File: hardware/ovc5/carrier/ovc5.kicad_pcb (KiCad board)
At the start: 2 copper layers, 6 parts, among them J1 USB_C_Receptacle, U1 Mercury_XU5_4CG-4EV-5EV, U2 CYUSB43x7, U3 PICAM_Expandable, U4 PICAM_Expandable, U5 USB3_A_Dual_Stacked

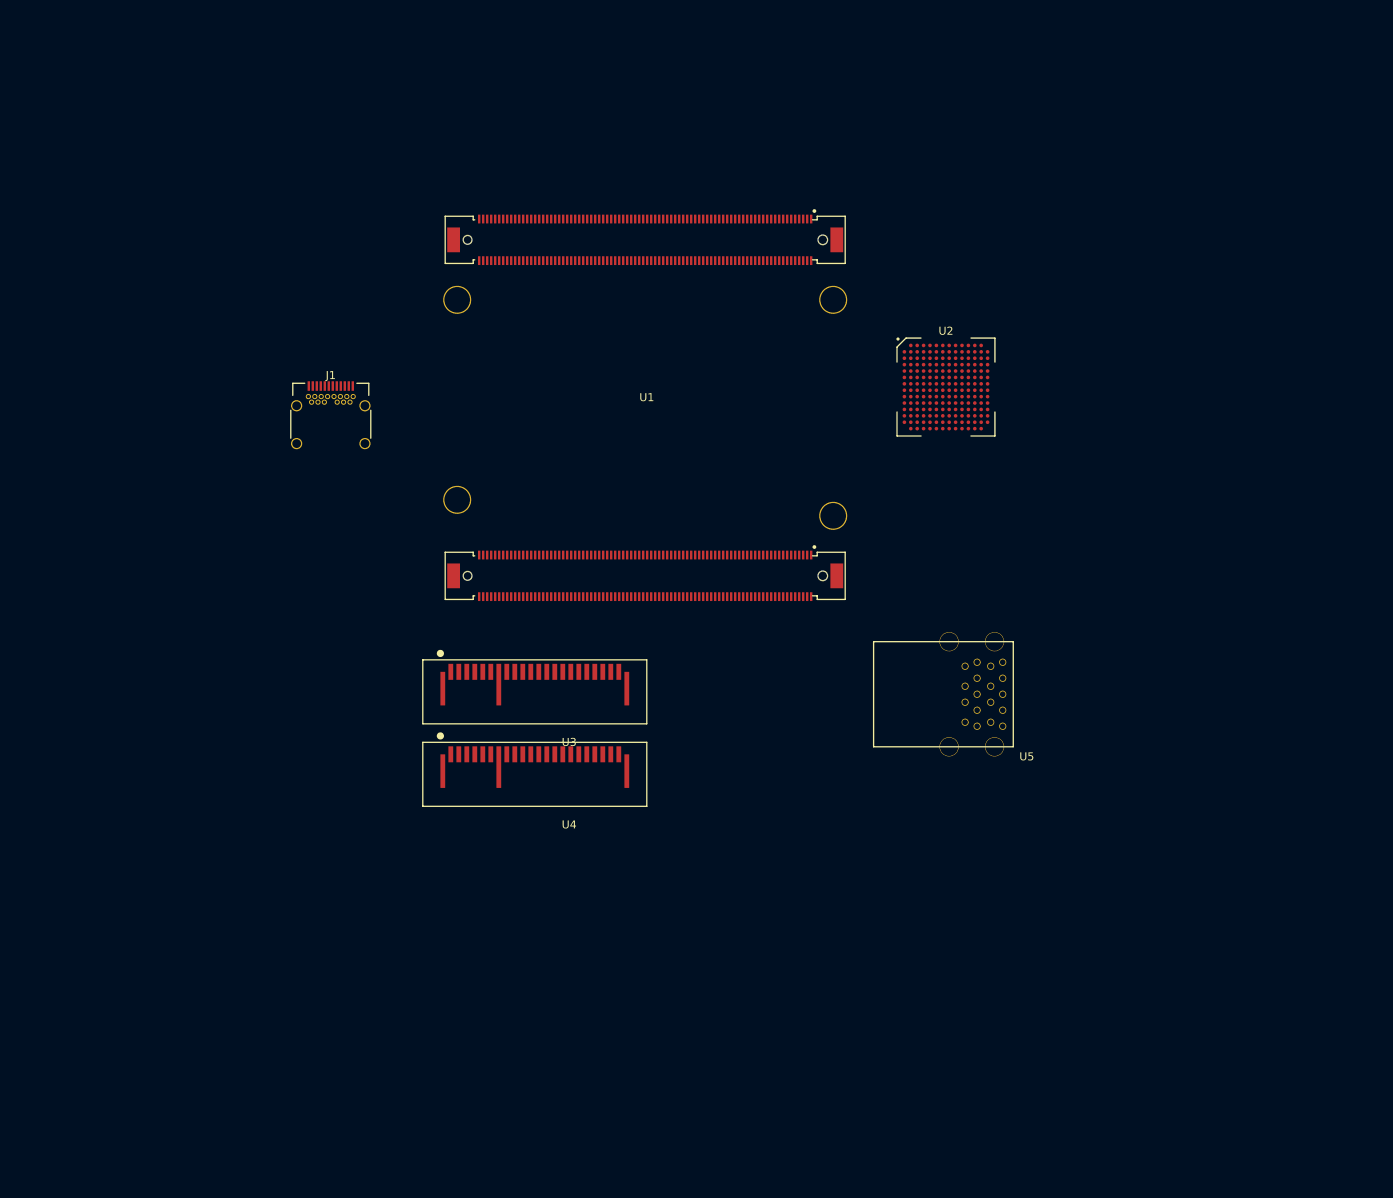
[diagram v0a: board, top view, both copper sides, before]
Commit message: Finish main schematics, start placing
Signed-off-by: Luca Della Vedova <luca@openrobotics.org>
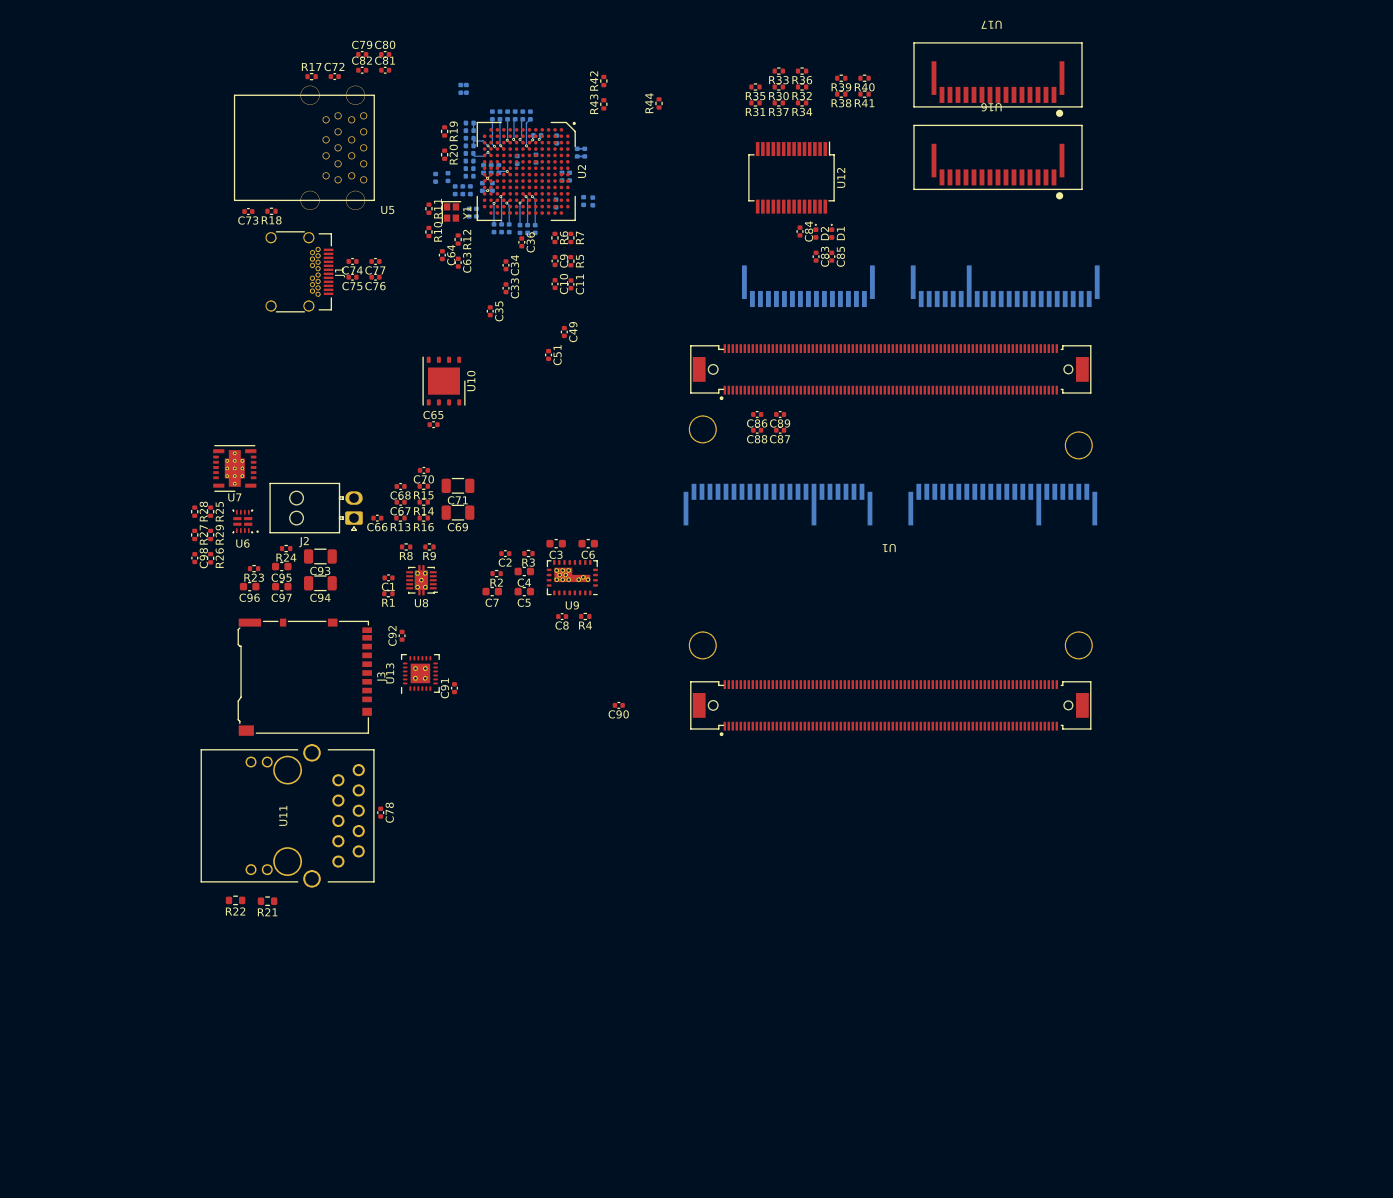
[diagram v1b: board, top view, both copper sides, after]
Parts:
- added C1: 100n, Capacitor_SMD:C_0402_1005Metric, F.Cu at (40.1, 77.8)
- added C10: 100n, Capacitor_SMD:C_0402_1005Metric, F.Cu at (60.9, 41.0)
- added C11: 100n, Capacitor_SMD:C_0402_1005Metric, F.Cu at (62.9, 41.1)
- added C12: 100n, Capacitor_SMD:C_0402_1005Metric, B.Cu at (54.0, 19.9)
- added C13: 100n, Capacitor_SMD:C_0402_1005Metric, B.Cu at (53.1, 19.9)
- added C14: 100n, Capacitor_SMD:C_0402_1005Metric, B.Cu at (56.0, 19.9)
- added C15: 100n, Capacitor_SMD:C_0402_1005Metric, B.Cu at (56.9, 19.9)
- added C16: 100n, Capacitor_SMD:C_0402_1005Metric, B.Cu at (56.5, 34.1)
- added C17: 100n, Capacitor_SMD:C_0402_1005Metric, B.Cu at (57.5, 34.1)
- added C18: 100n, Capacitor_SMD:C_0402_1005Metric, B.Cu at (53.3, 34.0)
- added C19: 100n, Capacitor_SMD:C_0402_1005Metric, B.Cu at (54.2, 34.0)
- added C2: 1u, Capacitor_SMD:C_0402_1005Metric, F.Cu at (54.7, 74.7)
- added C20: 100n, Capacitor_SMD:C_0402_1005Metric, B.Cu at (55.2, 34.0)
- added C21: 100n, Capacitor_SMD:C_0402_1005Metric, B.Cu at (55.0, 19.9)
- added C22: 100n, Capacitor_SMD:C_0402_1005Metric, B.Cu at (58.5, 34.1)
- added C23: 100n, Capacitor_SMD:C_0402_1005Metric, B.Cu at (57.9, 19.9)
- added C24: 100n, Capacitor_SMD:C_0402_1005Metric, B.Cu at (53.9, 26.6)
- added C25: 10u, Capacitor_SMD:C_0402_1005Metric, B.Cu at (53.1, 28.9)
- added C26: 10n, Capacitor_SMD:C_0402_1005Metric, B.Cu at (51.9, 28.9)
- added C27: 10n, Capacitor_SMD:C_0402_1005Metric, B.Cu at (53.0, 26.6)
- added C28: 10n, Capacitor_SMD:C_0402_1005Metric, B.Cu at (52.0, 26.6)
- added C29: 4u7, Capacitor_SMD:C_0402_1005Metric, B.Cu at (50.3, 22.8)
- added C3: 22u, Capacitor_SMD:C_0603_1608Metric, F.Cu at (61.1, 73.5)
- added C30: 100n, Capacitor_SMD:C_0402_1005Metric, B.Cu at (50.3, 23.8)
- added C31: 4u7, Capacitor_SMD:C_0402_1005Metric, B.Cu at (50.3, 20.9)
- added C32: 100n, Capacitor_SMD:C_0402_1005Metric, B.Cu at (50.3, 21.9)
- added C33: 1u, Capacitor_SMD:C_0402_1005Metric, F.Cu at (54.8, 41.5)
- added C34: 10u, Capacitor_SMD:C_0402_1005Metric, F.Cu at (54.8, 38.7)
- added C35: 1u, Capacitor_SMD:C_0402_1005Metric, F.Cu at (52.8, 44.4)
- added C36: 100n, Capacitor_SMD:C_0402_1005Metric, F.Cu at (56.8, 35.8)
- added C37: 100n, Capacitor_SMD:C_0402_1005Metric, B.Cu at (50.2, 24.7)
- added C38: 100n, Capacitor_SMD:C_0402_1005Metric, B.Cu at (50.2, 25.6)
- added C39: 100n, Capacitor_SMD:C_0402_1005Metric, B.Cu at (50.2, 26.6)
- added C4: 10p, Capacitor_SMD:C_0603_1608Metric, F.Cu at (57.1, 77.0)
- added C40: 100n, Capacitor_SMD:C_0402_1005Metric, B.Cu at (50.2, 27.6)
- added C41: 100n, Capacitor_SMD:C_0402_1005Metric, B.Cu at (61.1, 22.9)
- added C42: 100n, Capacitor_SMD:C_0402_1005Metric, B.Cu at (61.0, 30.9)
- added C43: 100n, Capacitor_SMD:C_0402_1005Metric, B.Cu at (46.0, 27.8)
- added C44: 100n, Capacitor_SMD:C_0402_1005Metric, B.Cu at (50.2, 32.1)
- added C45: 100n, Capacitor_SMD:C_0402_1005Metric, B.Cu at (49.4, 29.3)
- added C46: 10n, Capacitor_SMD:C_0402_1005Metric, B.Cu at (50.4, 29.3)
- added C47: 10u, Capacitor_SMD:C_0402_1005Metric, B.Cu at (48.5, 29.3)
- added C48: 100n, Capacitor_SMD:C_0402_1005Metric, B.Cu at (49.1, 16.6)
- added C49: 100n, Capacitor_SMD:C_0402_1005Metric, F.Cu at (62.1, 47.0)
- added C5: 22u, Capacitor_SMD:C_0603_1608Metric, F.Cu at (57.1, 79.5)
- added C50: 100n, Capacitor_SMD:C_0402_1005Metric, B.Cu at (58.7, 22.4)
- added C51: 10n, Capacitor_SMD:C_0402_1005Metric, F.Cu at (60.1, 49.9)
- added C52: 100n, Capacitor_SMD:C_0402_1005Metric, B.Cu at (64.5, 30.6)
- added C53: 100n, Capacitor_SMD:C_0402_1005Metric, B.Cu at (51.1, 32.1)
- added C54: 100n, Capacitor_SMD:C_0402_1005Metric, B.Cu at (49.9, 16.6)
- added C55: 1u, Capacitor_SMD:C_0402_1005Metric, B.Cu at (62.8, 27.6)
- added C56: 100n, Capacitor_SMD:C_0402_1005Metric, B.Cu at (61.8, 27.6)
- added C57: 100n, Capacitor_SMD:C_0402_1005Metric, B.Cu at (56.2, 25.5)
- added C58: 1u, Capacitor_SMD:C_0402_1005Metric, B.Cu at (64.7, 24.6)
- added C59: 100n, Capacitor_SMD:C_0402_1005Metric, B.Cu at (58.5, 25.4)
- added C6: 22u, Capacitor_SMD:C_0603_1608Metric, F.Cu at (65.1, 73.5)
- added C60: 100n, Capacitor_SMD:C_0402_1005Metric, B.Cu at (63.7, 24.6)
- added C61: 100n, Capacitor_SMD:C_0402_1005Metric, B.Cu at (65.7, 30.7)
- added C62: 4u7, Capacitor_SMD:C_0402_1005Metric, B.Cu at (47.5, 27.6)
- added C63: 12pF, Capacitor_SMD:C_0402_1005Metric, F.Cu at (48.8, 38.4)
- added C64: 12pF, Capacitor_SMD:C_0402_1005Metric, F.Cu at (46.8, 37.4)
- added C65: 100n, Capacitor_SMD:C_0402_1005Metric, F.Cu at (45.8, 58.6)
- added C66: 100n, Capacitor_SMD:C_0402_1005Metric, F.Cu at (38.7, 70.3)
- added C67: 100n, Capacitor_SMD:C_0402_1005Metric, F.Cu at (41.6, 68.3)
- added C68: 100n, Capacitor_SMD:C_0402_1005Metric, F.Cu at (41.6, 66.3)
- added C69: 100u, Capacitor_SMD:C_1206_3216Metric, F.Cu at (48.8, 69.6)
- added C7: 22u, Capacitor_SMD:C_0603_1608Metric, F.Cu at (53.1, 79.5)
- added C70: 100n, Capacitor_SMD:C_0402_1005Metric, F.Cu at (44.5, 64.3)
- added C71: 100u, Capacitor_SMD:C_1206_3216Metric, F.Cu at (48.8, 66.2)
- added C72: 2n2, Capacitor_SMD:C_0402_1005Metric, F.Cu at (33.4, 15.1)
- added C73: 2n2, Capacitor_SMD:C_0402_1005Metric, F.Cu at (22.6, 32.0)
- added C74: 100n, Capacitor_SMD:C_0402_1005Metric, F.Cu at (35.6, 38.2)
- added C75: 100n, Capacitor_SMD:C_0402_1005Metric, F.Cu at (35.6, 40.2)
- added C76: 100n, Capacitor_SMD:C_0402_1005Metric, F.Cu at (38.5, 40.2)
- added C77: 100n, Capacitor_SMD:C_0402_1005Metric, F.Cu at (38.5, 38.2)
- added C78: 100n, Capacitor_SMD:C_0402_1005Metric, F.Cu at (39.1, 107.1)
- added C79: 100n, Capacitor_SMD:C_0402_1005Metric, F.Cu at (36.8, 12.3)
- added C8: 100n, Capacitor_SMD:C_0402_1005Metric, F.Cu at (61.8, 82.6)
- added C80: 100n, Capacitor_SMD:C_0402_1005Metric, F.Cu at (39.7, 12.3)
- added C81: 100n, Capacitor_SMD:C_0402_1005Metric, F.Cu at (39.7, 14.3)
- added C82: 100n, Capacitor_SMD:C_0402_1005Metric, F.Cu at (36.8, 14.3)
- added C83: 100n, Capacitor_SMD:C_0402_1005Metric, F.Cu at (93.6, 37.6)
- added C84: 100n, Capacitor_SMD:C_0402_1005Metric, F.Cu at (91.5, 34.5)
- added C85: 100n, Capacitor_SMD:C_0402_1005Metric, F.Cu at (95.5, 37.6)
- added C86: 100n, Capacitor_SMD:C_0402_1005Metric, F.Cu at (86.2, 57.3)
- added C87: 100n, Capacitor_SMD:C_0402_1005Metric, F.Cu at (89.1, 59.3)
- added C88: 100n, Capacitor_SMD:C_0402_1005Metric, F.Cu at (86.2, 59.3)
- added C89: 100n, Capacitor_SMD:C_0402_1005Metric, F.Cu at (89.1, 57.3)
- added C9: 1u, Capacitor_SMD:C_0402_1005Metric, F.Cu at (60.9, 38.1)
- added C90: 1u, Capacitor_SMD:C_0402_1005Metric, F.Cu at (68.9, 93.7)
- added C91: 100n, Capacitor_SMD:C_0402_1005Metric, F.Cu at (48.4, 91.5)
- added C92: 100n, Capacitor_SMD:C_0402_1005Metric, F.Cu at (41.8, 85.0)
- added C93: 10u, Capacitor_SMD:C_1206_3216Metric, F.Cu at (31.6, 75.1)
- added C94: 10u, Capacitor_SMD:C_1206_3216Metric, F.Cu at (31.6, 78.4)
- added C95: 22u, Capacitor_SMD:C_0603_1608Metric, F.Cu at (26.8, 76.3)
- added C96: 22u, Capacitor_SMD:C_0603_1608Metric, F.Cu at (22.8, 78.8)
- added C97: 22u, Capacitor_SMD:C_0603_1608Metric, F.Cu at (26.8, 78.8)
- added C98: 100n, Capacitor_SMD:C_0402_1005Metric, F.Cu at (15.9, 75.3)
- added D1: LED_Small, LED_SMD:LED_0402_1005Metric, F.Cu at (95.5, 34.7)
- added D2: LED_Small, LED_SMD:LED_0402_1005Metric, F.Cu at (93.5, 34.7)
- added J2: AUX_PWR, Connector_Molex:Molex_Nano-Fit_105313-xx02_1x02_P2.50mm_Horizontal, F.Cu at (35.8, 70.3)
- added J3: Micro_SD_Card_Det_Hirose_DM3AT, Connector_Card:microSD_HC_Hirose_DM3AT-SF-PEJM5, F.Cu at (29.7, 90.2)
- added R1: 47k, Resistor_SMD:R_0402_1005Metric, F.Cu at (40.1, 79.7)
- added R10: 20k, Resistor_SMD:R_0402_1005Metric, F.Cu at (45.2, 34.5)
- added R11: 100k, Resistor_SMD:R_0402_1005Metric, F.Cu at (45.2, 31.6)
- added R12: 100k, Resistor_SMD:R_0402_1005Metric, F.Cu at (48.8, 35.5)
- added R13: 10k, Resistor_SMD:R_0402_1005Metric, F.Cu at (41.6, 70.3)
- added R14: 1k, Resistor_SMD:R_0402_1005Metric, F.Cu at (44.5, 68.3)
- added R15: 10k, Resistor_SMD:R_0402_1005Metric, F.Cu at (44.5, 66.3)
- added R16: 1k, Resistor_SMD:R_0402_1005Metric, F.Cu at (44.5, 70.3)
- added R17: 100k, Resistor_SMD:R_0402_1005Metric, F.Cu at (30.5, 15.1)
- added R18: 100k, Resistor_SMD:R_0402_1005Metric, F.Cu at (25.5, 31.9)
- added R19: 5k1, Resistor_SMD:R_0402_1005Metric, F.Cu at (47.1, 21.9)
- added R2: 348k, Resistor_SMD:R_0402_1005Metric, F.Cu at (53.6, 77.2)
- added R20: 5k1, Resistor_SMD:R_0402_1005Metric, F.Cu at (47.1, 24.9)
- added R21: 110R, Resistor_SMD:R_0603_1608Metric, F.Cu at (25.0, 118.2)
- added R22: 110R, Resistor_SMD:R_0603_1608Metric, F.Cu at (21.0, 118.1)
- added R23: 10k, Resistor_SMD:R_0402_1005Metric, F.Cu at (23.3, 76.6)
- added R24: 2k43, Resistor_SMD:R_0402_1005Metric, F.Cu at (27.3, 74.1)
- added R25: 47k, Resistor_SMD:R_0402_1005Metric, F.Cu at (17.9, 69.5)
- added R26: 10k, Resistor_SMD:R_0402_1005Metric, F.Cu at (17.9, 75.3)
- added R27: 47k, Resistor_SMD:R_0402_1005Metric, F.Cu at (15.9, 72.4)
- added R28: 10k, Resistor_SMD:R_0402_1005Metric, F.Cu at (15.9, 69.5)
- added R29: 22k, Resistor_SMD:R_0402_1005Metric, F.Cu at (17.9, 72.4)
- added R3: 348k, Resistor_SMD:R_0402_1005Metric, F.Cu at (57.6, 74.7)
- added R30: 2k4, Resistor_SMD:R_0402_1005Metric, F.Cu at (88.9, 16.4)
- added R31: 2k4, Resistor_SMD:R_0402_1005Metric, F.Cu at (86.0, 18.4)
- added R32: 2k4, Resistor_SMD:R_0402_1005Metric, F.Cu at (91.8, 16.4)
- added R33: 2k4, Resistor_SMD:R_0402_1005Metric, F.Cu at (88.9, 14.4)
- added R34: 2k4, Resistor_SMD:R_0402_1005Metric, F.Cu at (91.8, 18.4)
- added R35: 2k4, Resistor_SMD:R_0402_1005Metric, F.Cu at (86.0, 16.4)
- added R36: 2k4, Resistor_SMD:R_0402_1005Metric, F.Cu at (91.8, 14.4)
- added R37: 2k4, Resistor_SMD:R_0402_1005Metric, F.Cu at (88.9, 18.4)
- added R38: 2k4, Resistor_SMD:R_0402_1005Metric, F.Cu at (96.7, 17.3)
- added R39: 2k4, Resistor_SMD:R_0402_1005Metric, F.Cu at (96.7, 15.3)
- added R4: 100k, Resistor_SMD:R_0402_1005Metric, F.Cu at (64.7, 82.6)
- added R40: 2k4, Resistor_SMD:R_0402_1005Metric, F.Cu at (99.6, 15.3)
- added R41: 2k4, Resistor_SMD:R_0402_1005Metric, F.Cu at (99.6, 17.3)
- added R42: 2k4, Resistor_SMD:R_0402_1005Metric, F.Cu at (67.0, 15.7)
- added R43: 2k4, Resistor_SMD:R_0402_1005Metric, F.Cu at (67.0, 18.6)
- added R44: 10k, Resistor_SMD:R_0402_1005Metric, F.Cu at (73.9, 18.4)
- added R5: 20k, Resistor_SMD:R_0402_1005Metric, F.Cu at (62.9, 38.2)
- added R6: 10k, Resistor_SMD:R_0402_1005Metric, F.Cu at (60.9, 35.3)
- added R7: 10k, Resistor_SMD:R_0402_1005Metric, F.Cu at (62.9, 35.3)
- added R8: 100k, Resistor_SMD:R_0402_1005Metric, F.Cu at (42.3, 73.9)
- added R9: 100k, Resistor_SMD:R_0402_1005Metric, F.Cu at (45.2, 73.9)
- added U10: S25FL064, Package_SON:WSON-8-1EP_6x5mm_P1.27mm_EP3.4x4mm, F.Cu at (47.0, 53.2)
- added U11: ARJ11C-MBSAS-A-BA-7MU2, Ethernet:ARJ11C-MBSAS-A-BA-7MU2, F.Cu at (27.5, 107.5)
- added U12: FT232RL, Package_SO:SSOP-28_5.3x10.2mm_P0.65mm, F.Cu at (90.5, 27.8)
- added U13: TXS02612, WQFN:TI_RTW0024B, F.Cu at (44.1, 89.7)
- added U14: PICAM, Connectors_OSRF:AMPHENOL_SFW15R, B.Cu at (92.4, 39.8)
- added U15: PICAM_Expandable, Connectors_OSRF:AMPHENOL_SFW15R+SFW21R, B.Cu at (88.9, 70.0)
- added U16: PICAM, Connectors_OSRF:AMPHENOL_SFW15R, F.Cu at (116.5, 24.6)
- added U17: PICAM, Connectors_OSRF:AMPHENOL_SFW15R, F.Cu at (116.5, 14.3)
- added U6: TPS2121, TI:Texas_VQFN-HR-12_2x2.5_Pitch0.5mm, F.Cu at (21.9, 70.7)
- added U7: TPSM53604RDA, Package_DFN_QFN:Texas_B3QFN-14-1EP_5x5.5mm_P0.65mm_ThermalVia, F.Cu at (20.9, 64.1)
- added U8: TPS2561, Package_SON:VSON-10-1EP_3x3mm_P0.5mm_EP1.65x2.4mm_ThermalVias, F.Cu at (44.2, 78.0)
- added U9: EN5339QI, DCDC:Converter_DCDC_Intel_QFN-24_4x6mm_P0.65mm_ThermalVias, F.Cu at (63.1, 77.7)
- added Y1: 25MHz, Crystal:Crystal_SMD_2016-4Pin_2.0x1.6mm, F.Cu at (48.0, 32.1)
- U3, U4: moved to B.Cu
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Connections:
- net Net-(J1-PadA4) renamed VBUS
- J1 pad A1: Net-(J1-PadA1) -> GND
- J1 pad A10: unconnected-(J1-PadA10) -> /USB/USB_DS_RX2_N
- J1 pad A11: unconnected-(J1-PadA11) -> /USB/USB_DS_RX2_P
- J1 pad A12: Net-(J1-PadA1) -> GND
- J1 pad A2: unconnected-(J1-PadA2) -> Net-(J1-PadA2)
- J1 pad A3: unconnected-(J1-PadA3) -> Net-(J1-PadA3)
- J1 pad A5: unconnected-(J1-PadA5) -> /USB/USB_DS_CC1
- J1 pad A6: unconnected-(J1-PadA6) -> /USB/USB_DS_D_P
- J1 pad A7: unconnected-(J1-PadA7) -> /USB/USB_DS_D_N
- J1 pad B1: Net-(J1-PadA1) -> GND
- J1 pad B10: unconnected-(J1-PadB10) -> /USB/USB_DS_RX1_N
- J1 pad B11: unconnected-(J1-PadB11) -> /USB/USB_DS_RX1_P
- J1 pad B12: Net-(J1-PadA1) -> GND
- J1 pad B2: unconnected-(J1-PadB2) -> Net-(J1-PadB2)
- J1 pad B3: unconnected-(J1-PadB3) -> Net-(J1-PadB3)
- J1 pad B5: unconnected-(J1-PadB5) -> /USB/USB_DS_CC2
- J1 pad B6: unconnected-(J1-PadB6) -> /USB/USB_DS_D_P
- J1 pad B7: unconnected-(J1-PadB7) -> /USB/USB_DS_D_N
- J1 pad S1: unconnected-(J1-PadS1) -> Net-(C73-Pad1)
- U1 pad A101: unconnected-(U1-PadA101) -> SDIO_D2
- U1 pad A103: unconnected-(U1-PadA103) -> SDIO_D3
- U1 pad A105: unconnected-(U1-PadA105) -> DEBUG_UART_RX
- U1 pad A107: unconnected-(U1-PadA107) -> DEBUG_UART_TX
- U1 pad A108: unconnected-(U1-PadA108) -> GND
- U1 pad A109: unconnected-(U1-PadA109) -> GND
- U1 pad A120: unconnected-(U1-PadA120) -> GND
- U1 pad A125: unconnected-(U1-PadA125) -> GND
- U1 pad A127: unconnected-(U1-PadA127) -> FPGA_USB0_D+
- U1 pad A129: unconnected-(U1-PadA129) -> FPGA_USB0_D-
- U1 pad A13: unconnected-(U1-PadA13) -> GND
- U1 pad A131: unconnected-(U1-PadA131) -> FPGA_USB1_D+
- U1 pad A133: unconnected-(U1-PadA133) -> FPGA_USB1_D-
- U1 pad A134: unconnected-(U1-PadA134) -> GND
- U1 pad A135: unconnected-(U1-PadA135) -> GND
- U1 pad A138: unconnected-(U1-PadA138) -> GND
- U1 pad A139: unconnected-(U1-PadA139) -> GND
- U1 pad A14: unconnected-(U1-PadA14) -> GND
- U1 pad A142: unconnected-(U1-PadA142) -> GND
- U1 pad A143: unconnected-(U1-PadA143) -> GND
- U1 pad A145: unconnected-(U1-PadA145) -> GBE_MDI3_N
- U1 pad A147: unconnected-(U1-PadA147) -> CAM3_DAT3-
- U1 pad A149: unconnected-(U1-PadA149) -> GBE_LED_ACT
- U1 pad A151: unconnected-(U1-PadA151) -> GBE_MDI2_N
- U1 pad A153: unconnected-(U1-PadA153) -> GBE_MDI2_P
- U1 pad A157: unconnected-(U1-PadA157) -> GBE_MDI1_N
- U1 pad A159: unconnected-(U1-PadA159) -> GBE_MDI1_P
- U1 pad A161: unconnected-(U1-PadA161) -> GBE_LED_LINK
- U1 pad A163: unconnected-(U1-PadA163) -> GBE_MDI0_N
- U1 pad A165: unconnected-(U1-PadA165) -> GBE_MDI0_P
- U1 pad A166: unconnected-(U1-PadA166) -> GND
- U1 pad A167: unconnected-(U1-PadA167) -> GND
- U1 pad A20: unconnected-(U1-PadA20) -> GND
- U1 pad A23: unconnected-(U1-PadA23) -> GND
- U1 pad A26: unconnected-(U1-PadA26) -> +3V3
- U1 pad A29: unconnected-(U1-PadA29) -> +3V3
- U1 pad A32: unconnected-(U1-PadA32) -> GND
- U1 pad A35: unconnected-(U1-PadA35) -> GND
- U1 pad A44: unconnected-(U1-PadA44) -> GND
- U1 pad A47: unconnected-(U1-PadA47) -> GND
- U1 pad A50: unconnected-(U1-PadA50) -> +3V3
- U1 pad A56: unconnected-(U1-PadA56) -> GND
- U1 pad A59: unconnected-(U1-PadA59) -> GND
- U1 pad A68: unconnected-(U1-PadA68) -> GND
- U1 pad A71: unconnected-(U1-PadA71) -> GND
- U1 pad A80: unconnected-(U1-PadA80) -> GND
- U1 pad A83: unconnected-(U1-PadA83) -> GND
- U1 pad A86: unconnected-(U1-PadA86) -> +3V3
- U1 pad A91: unconnected-(U1-PadA91) -> SDIO_CLK
- U1 pad A92: unconnected-(U1-PadA92) -> CAM3_SDA
- U1 pad A93: unconnected-(U1-PadA93) -> SDIO_CMD
- U1 pad A94: unconnected-(U1-PadA94) -> CAM3_SCL
- U1 pad A95: unconnected-(U1-PadA95) -> SDIO_D0
- U1 pad A96: unconnected-(U1-PadA96) -> GND
- U1 pad A97: unconnected-(U1-PadA97) -> SDIO_D1
- U1 pad A99: unconnected-(U1-PadA99) -> GND
- U1 pad B1: unconnected-(U1-PadB1) -> GND
- U1 pad B100: unconnected-(U1-PadB100) -> CAM4_CLK+
- U1 pad B101: unconnected-(U1-PadB101) -> CAM0_CLK+
- U1 pad B102: unconnected-(U1-PadB102) -> CAM4_CLK-
- U1 pad B103: unconnected-(U1-PadB103) -> CAM0_CLK-
- U1 pad B104: unconnected-(U1-PadB104) -> CAM1_TRIGGER
- U1 pad B105: unconnected-(U1-PadB105) -> GND
- U1 pad B106: unconnected-(U1-PadB106) -> CAM1_ENABLE
- U1 pad B107: unconnected-(U1-PadB107) -> CAM0_DAT0+
- U1 pad B108: unconnected-(U1-PadB108) -> +1V8
- U1 pad B109: unconnected-(U1-PadB109) -> CAM0_DAT0-
- U1 pad B11: unconnected-(U1-PadB11) -> GND
- U1 pad B110: unconnected-(U1-PadB110) -> CAM1_CLK+
- U1 pad B111: unconnected-(U1-PadB111) -> CAM0_DAT1+
- U1 pad B112: unconnected-(U1-PadB112) -> CAM1_CLK-
- U1 pad B113: unconnected-(U1-PadB113) -> CAM0_DAT1-
- U1 pad B114: unconnected-(U1-PadB114) -> CAM1_DAT0+
- U1 pad B115: unconnected-(U1-PadB115) -> +3V3
- U1 pad B116: unconnected-(U1-PadB116) -> CAM1_DAT0-
- U1 pad B117: unconnected-(U1-PadB117) -> CAM0_DAT3+
- U1 pad B118: unconnected-(U1-PadB118) -> GND
- U1 pad B119: unconnected-(U1-PadB119) -> CAM0_DAT3-
- U1 pad B120: unconnected-(U1-PadB120) -> CAM1_DAT1+
- U1 pad B121: unconnected-(U1-PadB121) -> GND
- U1 pad B122: unconnected-(U1-PadB122) -> CAM1_DAT1-
- U1 pad B123: unconnected-(U1-PadB123) -> CAM3_CLK+
- U1 pad B124: unconnected-(U1-PadB124) -> CAM1_SDA
- U1 pad B125: unconnected-(U1-PadB125) -> CAM3_CLK-
- U1 pad B126: unconnected-(U1-PadB126) -> CAM1_SCL
- U1 pad B127: unconnected-(U1-PadB127) -> +3V3
- U1 pad B128: unconnected-(U1-PadB128) -> +1V8
- U1 pad B129: unconnected-(U1-PadB129) -> CAM0_DAT2+
- U1 pad B130: unconnected-(U1-PadB130) -> CAM2_CLK+
- U1 pad B131: unconnected-(U1-PadB131) -> CAM0_DAT2-
- U1 pad B132: unconnected-(U1-PadB132) -> CAM2_CLK-
- U1 pad B133: unconnected-(U1-PadB133) -> CAM3_ENABLE
- U1 pad B134: unconnected-(U1-PadB134) -> GND
- U1 pad B135: unconnected-(U1-PadB135) -> CAM3_TRIGGER
- U1 pad B136: unconnected-(U1-PadB136) -> CAM1_DAT2+
- U1 pad B137: unconnected-(U1-PadB137) -> GND
- U1 pad B138: unconnected-(U1-PadB138) -> CAM1_DAT2-
- U1 pad B139: unconnected-(U1-PadB139) -> CAM2_SCL
- U1 pad B14: unconnected-(U1-PadB14) -> GND
- U1 pad B141: unconnected-(U1-PadB141) -> CAM2_SDA
- U1 pad B142: unconnected-(U1-PadB142) -> CAM1_DAT3+
- U1 pad B143: unconnected-(U1-PadB143) -> +1V8
- U1 pad B144: unconnected-(U1-PadB144) -> CAM1_DAT3-
- U1 pad B145: unconnected-(U1-PadB145) -> CAM3_DAT3+
- U1 pad B146: unconnected-(U1-PadB146) -> GND
- U1 pad B148: unconnected-(U1-PadB148) -> CAM4_DAT1+
- U1 pad B149: unconnected-(U1-PadB149) -> GND
- U1 pad B15: unconnected-(U1-PadB15) -> GND
- U1 pad B150: unconnected-(U1-PadB150) -> CAM4_DAT1-
- U1 pad B151: unconnected-(U1-PadB151) -> CAM3_DAT0+
- U1 pad B152: unconnected-(U1-PadB152) -> +3V3
- U1 pad B153: unconnected-(U1-PadB153) -> CAM3_DAT0-
- U1 pad B154: unconnected-(U1-PadB154) -> CAM2_DAT0+
- U1 pad B155: unconnected-(U1-PadB155) -> +3V3
- U1 pad B156: unconnected-(U1-PadB156) -> CAM2_DAT0-
- U1 pad B157: unconnected-(U1-PadB157) -> CAM3_DAT2+
- U1 pad B158: unconnected-(U1-PadB158) -> GND
- U1 pad B159: unconnected-(U1-PadB159) -> CAM3_DAT2-
- U1 pad B160: unconnected-(U1-PadB160) -> CAM2_DAT1+
- U1 pad B161: unconnected-(U1-PadB161) -> GND
- U1 pad B162: unconnected-(U1-PadB162) -> CAM2_DAT1-
- U1 pad B163: unconnected-(U1-PadB163) -> CAM3_DAT1+
- U1 pad B164: unconnected-(U1-PadB164) -> CAM4_DAT0+
- U1 pad B165: unconnected-(U1-PadB165) -> CAM3_DAT1-
- U1 pad B166: unconnected-(U1-PadB166) -> CAM4_DAT0-
- U1 pad B18: unconnected-(U1-PadB18) -> GND
- U1 pad B19: unconnected-(U1-PadB19) -> GND
- U1 pad B2: unconnected-(U1-PadB2) -> GND
- U1 pad B22: unconnected-(U1-PadB22) -> GND
- U1 pad B23: unconnected-(U1-PadB23) -> GND
- U1 pad B26: unconnected-(U1-PadB26) -> GND
- U1 pad B27: unconnected-(U1-PadB27) -> GND
- U1 pad B29: unconnected-(U1-PadB29) -> Net-(C86-Pad2)
- U1 pad B30: unconnected-(U1-PadB30) -> GND
- U1 pad B31: unconnected-(U1-PadB31) -> GND
- U1 pad B32: unconnected-(U1-PadB32) -> FPGA_USB0_RX+
- U1 pad B33: unconnected-(U1-PadB33) -> Net-(C87-Pad2)
- U1 pad B34: unconnected-(U1-PadB34) -> GND
- U1 pad B35: unconnected-(U1-PadB35) -> GND
- U1 pad B36: unconnected-(U1-PadB36) -> FPGA_USB0_RX-
- U1 pad B37: unconnected-(U1-PadB37) -> Net-(C88-Pad2)
- U1 pad B38: unconnected-(U1-PadB38) -> GND
- U1 pad B39: unconnected-(U1-PadB39) -> GND
- U1 pad B40: unconnected-(U1-PadB40) -> FPGA_USB1_RX+
- U1 pad B41: unconnected-(U1-PadB41) -> Net-(C89-Pad2)
- U1 pad B42: unconnected-(U1-PadB42) -> GND
- U1 pad B43: unconnected-(U1-PadB43) -> GND
- U1 pad B44: unconnected-(U1-PadB44) -> FPGA_USB1_RX-
- U1 pad B46: unconnected-(U1-PadB46) -> GND
- U1 pad B49: unconnected-(U1-PadB49) -> GND
- U1 pad B52: unconnected-(U1-PadB52) -> +1V8
- U1 pad B55: unconnected-(U1-PadB55) -> +3V3
- U1 pad B58: unconnected-(U1-PadB58) -> GND
- U1 pad B61: unconnected-(U1-PadB61) -> GND
- U1 pad B64: unconnected-(U1-PadB64) -> +1V8
- U1 pad B70: unconnected-(U1-PadB70) -> GND
- U1 pad B72: unconnected-(U1-PadB72) -> CAM2_TRIGGER
- U1 pad B73: unconnected-(U1-PadB73) -> GND
- U1 pad B74: unconnected-(U1-PadB74) -> CAM2_ENABLE
- U1 pad B75: unconnected-(U1-PadB75) -> CAM5_ENABLE
- U1 pad B76: unconnected-(U1-PadB76) -> +1V8
- U1 pad B77: unconnected-(U1-PadB77) -> CAM5_TRIGGER
- U1 pad B78: unconnected-(U1-PadB78) -> CAM5_SDA
- U1 pad B79: unconnected-(U1-PadB79) -> +3V3
- U1 pad B80: unconnected-(U1-PadB80) -> CAM5_SCL
- U1 pad B81: unconnected-(U1-PadB81) -> CAM4_ENABLE
- U1 pad B82: unconnected-(U1-PadB82) -> GND
- U1 pad B83: unconnected-(U1-PadB83) -> CAM4_TRIGGER
- U1 pad B84: unconnected-(U1-PadB84) -> CAM5_CLK+
- U1 pad B85: unconnected-(U1-PadB85) -> GND
- U1 pad B86: unconnected-(U1-PadB86) -> CAM5_CLK-
- U1 pad B87: unconnected-(U1-PadB87) -> CAM4_SCL
- U1 pad B88: unconnected-(U1-PadB88) -> +1V8
- U1 pad B89: unconnected-(U1-PadB89) -> CAM4_SDA
- U1 pad B90: unconnected-(U1-PadB90) -> CAM5_DAT0+
- U1 pad B91: unconnected-(U1-PadB91) -> CAM0_SCL
- U1 pad B92: unconnected-(U1-PadB92) -> CAM5_DAT0-
- U1 pad B93: unconnected-(U1-PadB93) -> CAM0_SDA
- U1 pad B94: unconnected-(U1-PadB94) -> CAM5_DAT1+
- U1 pad B95: unconnected-(U1-PadB95) -> +1V8
- U1 pad B96: unconnected-(U1-PadB96) -> CAM5_DAT1-
- U1 pad B97: unconnected-(U1-PadB97) -> CAM0_ENABLE
- U1 pad B98: unconnected-(U1-PadB98) -> GND
- U1 pad B99: unconnected-(U1-PadB99) -> CAM0_TRIGGER
- U2 pad A10: unconnected-(U2-PadA10) -> /USB/USB_SPI_DO
- U2 pad A11: unconnected-(U2-PadA11) -> /USB/USB_SP_nWP
- U2 pad A12: unconnected-(U2-PadA12) -> USB_UART_D-
- U2 pad A13: unconnected-(U2-PadA13) -> USB_UART_D+
- U2 pad A5: unconnected-(U2-PadA5) -> +3V3
- U2 pad A6: unconnected-(U2-PadA6) -> Net-(U2-PadA6)
- U2 pad A7: unconnected-(U2-PadA7) -> Net-(U2-PadA7)
- U2 pad B1: unconnected-(U2-PadB1) -> FPGA_USB0_D-
- U2 pad B10: unconnected-(U2-PadB10) -> /USB/USB_SPI_CS
- U2 pad B13: unconnected-(U2-PadB13) -> FPGA_USB1_D-
- U2 pad B14: unconnected-(U2-PadB14) -> FPGA_USB1_D+
- U2 pad B2: unconnected-(U2-PadB2) -> FPGA_USB0_D+
- U2 pad B3: unconnected-(U2-PadB3) -> /USB/USB_DS_CC2
- U2 pad B5: unconnected-(U2-PadB5) -> /USB/VBUS_MON_P1
- U2 pad B6: unconnected-(U2-PadB6) -> Net-(U2-PadB6)
- U2 pad C1: unconnected-(U2-PadC1) -> FPGA_USB0_TX+
- U2 pad C11: unconnected-(U2-PadC11) -> /USB/XRES_DMC
- U2 pad C12: unconnected-(U2-PadC12) -> +3V3
- U2 pad C2: unconnected-(U2-PadC2) -> FPGA_USB0_TX-
- U2 pad C3: unconnected-(U2-PadC3) -> +3V3
- U2 pad C4: unconnected-(U2-PadC4) -> +5V
- U2 pad C6: unconnected-(U2-PadC6) -> +3V3
- U2 pad C9: unconnected-(U2-PadC9) -> +3V3
- U2 pad D1: unconnected-(U2-PadD1) -> FPGA_USB0_RX+
- U2 pad D11: unconnected-(U2-PadD11) -> /USB/USB_I2C_SDA
- U2 pad D12: unconnected-(U2-PadD12) -> /USB/USB_SPI_CLK
- U2 pad D2: unconnected-(U2-PadD2) -> FPGA_USB0_RX-
- U2 pad D3: unconnected-(U2-PadD3) -> /USB/USB_DS_CC1
- U2 pad D4: unconnected-(U2-PadD4) -> /USB/VBUS_MON_P0
- U2 pad D5: unconnected-(U2-PadD5) -> Net-(U2-PadD5)
- U2 pad D7: unconnected-(U2-PadD7) -> +5V
- U2 pad D8: unconnected-(U2-PadD8) -> /USB/USB_US0_CC1
- U2 pad D9: unconnected-(U2-PadD9) -> Net-(U2-PadD9)
- U2 pad E10: unconnected-(U2-PadE10) -> GND
- U2 pad E11: unconnected-(U2-PadE11) -> /USB/USB_I2C_SCL
- U2 pad E13: unconnected-(U2-PadE13) -> FPGA_USB1_RX-
- U2 pad E14: unconnected-(U2-PadE14) -> FPGA_USB1_RX+
- U2 pad E7: unconnected-(U2-PadE7) -> +5V
- U2 pad E8: unconnected-(U2-PadE8) -> +3V3
- U2 pad F10: unconnected-(U2-PadF10) -> +3V3
- U2 pad F11: unconnected-(U2-PadF11) -> /USB/VDD10
- U2 pad F12: unconnected-(U2-PadF12) -> /USB/USB_SPI_DI
- U2 pad F13: unconnected-(U2-PadF13) -> FPGA_USB1_TX-
- U2 pad F14: unconnected-(U2-PadF14) -> FPGA_USB1_TX+
- U2 pad F4: unconnected-(U2-PadF4) -> /USB/VDD10
- U2 pad F5: unconnected-(U2-PadF5) -> Net-(U2-PadD5)
- U2 pad F6: unconnected-(U2-PadF6) -> GND
- U2 pad F7: unconnected-(U2-PadF7) -> GND
- U2 pad F8: unconnected-(U2-PadF8) -> GND
- U2 pad F9: unconnected-(U2-PadF9) -> GND
- U2 pad G1: unconnected-(U2-PadG1) -> /USB/USB_H1_TX_P
- U2 pad G10: unconnected-(U2-PadG10) -> /USB/USB_I2C_SDA
- U2 pad G11: unconnected-(U2-PadG11) -> /USB/1V0_PHY
- U2 pad G12: unconnected-(U2-PadG12) -> +3V3
- U2 pad G13: unconnected-(U2-PadG13) -> /USB/USB_H0_RX_N
- U2 pad G14: unconnected-(U2-PadG14) -> /USB/USB_H0_RX_P
- U2 pad G2: unconnected-(U2-PadG2) -> /USB/USB_H1_TX_N
- U2 pad G3: unconnected-(U2-PadG3) -> +3V3
- U2 pad G4: unconnected-(U2-PadG4) -> /USB/1V0_PHY
- U2 pad G5: unconnected-(U2-PadG5) -> +3V3
- U2 pad G6: unconnected-(U2-PadG6) -> GND
- U2 pad G7: unconnected-(U2-PadG7) -> GND
- U2 pad G8: unconnected-(U2-PadG8) -> GND
- U2 pad G9: unconnected-(U2-PadG9) -> GND
- U2 pad H1: unconnected-(U2-PadH1) -> /USB/USB_H1_RX_P
- U2 pad H10: unconnected-(U2-PadH10) -> +3V3
- U2 pad H11: unconnected-(U2-PadH11) -> /USB/1V0_PHY
- U2 pad H12: unconnected-(U2-PadH12) -> /USB/1V0_PHY
- U2 pad H13: unconnected-(U2-PadH13) -> /USB/USB_H0_TX_N
- U2 pad H14: unconnected-(U2-PadH14) -> /USB/USB_H0_TX_P
- U2 pad H2: unconnected-(U2-PadH2) -> /USB/USB_H1_RX_N
- U2 pad H3: unconnected-(U2-PadH3) -> /USB/1V0_PHY
- U2 pad H5: unconnected-(U2-PadH5) -> /USB/USB_SPI_DI
- U2 pad H6: unconnected-(U2-PadH6) -> GND
- U2 pad H7: unconnected-(U2-PadH7) -> GND
- U2 pad H8: unconnected-(U2-PadH8) -> GND
- U2 pad H9: unconnected-(U2-PadH9) -> GND
- U2 pad J1: unconnected-(U2-PadJ1) -> /USB/USB_H1_D_N
- U2 pad J11: unconnected-(U2-PadJ11) -> /USB/VDD10
- U2 pad J12: unconnected-(U2-PadJ12) -> +3V3
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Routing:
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
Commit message: Place and route USB and MIPI lanes
Signed-off-by: Luca Della Vedova <luca@openrobotics.org>
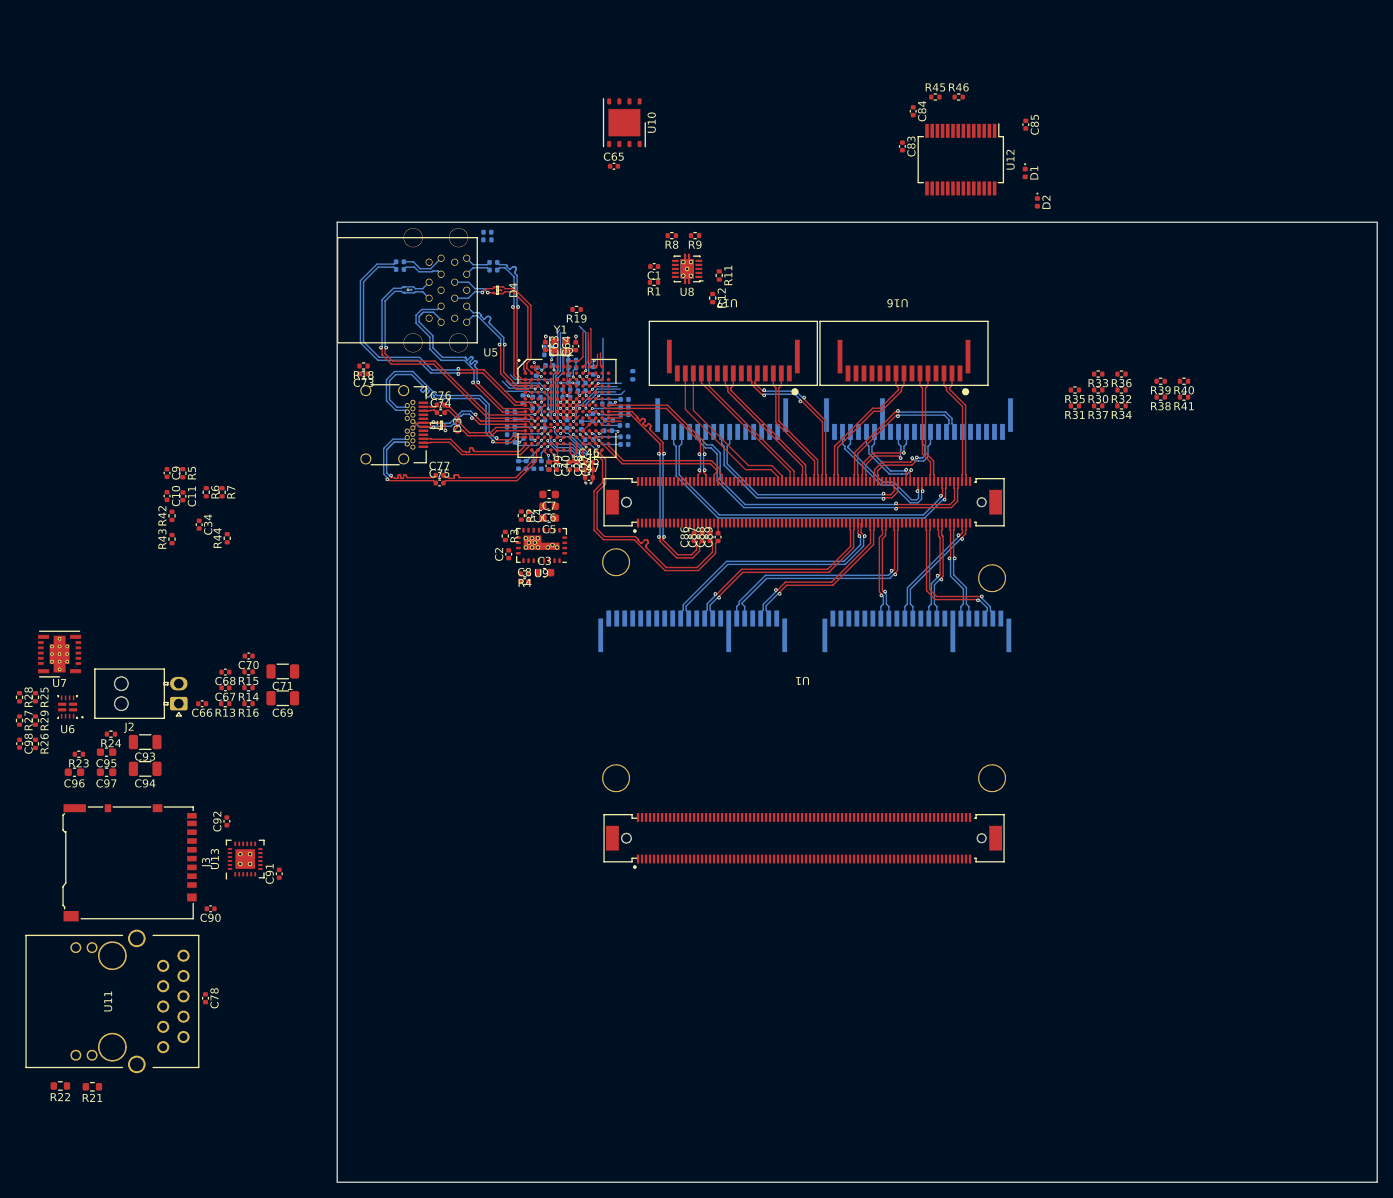
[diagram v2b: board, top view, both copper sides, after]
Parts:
- removed C23: 100n, Capacitor_SMD:C_0402_1005Metric
- added D3: D_TVS_Dual_AAC, USB:TPD2EUSB30x, F.Cu at (46.8, 58.7)
- added D4: D_TVS_Dual_AAC, USB:TPD2EUSB30x, F.Cu at (53.8, 41.8)
- added D5: D_TVS_Dual_AAC, USB:TPD2EUSB30x, B.Cu at (42.5, 41.8)
- added R45: 220R, Resistor_SMD:R_0402_1005Metric, F.Cu at (108.5, 17.6)
- added R46: 220R, Resistor_SMD:R_0402_1005Metric, F.Cu at (111.4, 17.6)
- C27, C28, C39, C40, C45, C46, C47: moved to F.Cu
- C33, C35, C36, C49, C51, C72, C79, C80, C81, C82, R10, R17, R20: moved to B.Cu
- C4: footprint Capacitor_SMD:C_0603_1608Metric -> Capacitor_SMD:C_0402_1005Metric
- moved R42 76.6 mm to (13.1, 70.0)
- moved R43 76.6 mm to (13.1, 72.9)
- moved R44 76.6 mm to (20.0, 72.8)
- moved C90 57.0 mm to (17.9, 119.1)
- moved C9 55.3 mm to (12.4, 64.7)
- moved C10 55.3 mm to (12.4, 67.5)
- moved C11 55.3 mm to (14.4, 67.6)
- moved R5 55.3 mm to (14.4, 64.7)
- moved R30 55.0 mm to (128.8, 54.3)
- moved R31 55.0 mm to (125.9, 56.3)
- moved R32 55.0 mm to (131.7, 54.3)
- moved R33 55.0 mm to (128.8, 52.3)
- moved R34 55.0 mm to (131.7, 56.3)
- moved R35 55.0 mm to (125.9, 54.3)
- moved R36 55.0 mm to (131.7, 52.3)
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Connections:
- net Net-(J1-PadA2) renamed /USB/USB_DS_TX1_CONN_N
- net Net-(J1-PadA3) renamed /USB/USB_DS_TX1_CONN_P
- net Net-(J1-PadB2) renamed /USB/USB_DS_TX2_CONN_N
- net Net-(J1-PadB3) renamed /USB/USB_DS_TX2_CONN_P
- C63 pad 2: Net-(U2-PadA6) -> Net-(C63-Pad2)
- C64 pad 1: Net-(U2-PadA7) -> Net-(C64-Pad1)
- C74 pad 2: /USB/USB_DS_TX1_N -> /USB/USB_DS_TX1_P
- C75 pad 2: /USB/USB_DS_TX2_N -> /USB/USB_DS_TX2_P
- C76 pad 2: /USB/USB_DS_TX1_P -> /USB/USB_DS_TX1_N
- C77 pad 2: /USB/USB_DS_TX2_P -> /USB/USB_DS_TX2_N
- C79 pad 1: Net-(U5-Pad8) -> /USB/USB_H0_TX_CONN_N
- C80 pad 1: Net-(U5-Pad17) -> /USB/USB_H1_TX_CONN_N
- C81 pad 1: Net-(U5-Pad9) -> /USB/USB_H0_TX_CONN_P
- C82 pad 1: Net-(U5-Pad18) -> /USB/USB_H1_TX_CONN_P
- D1 pad 2: +3V3 -> Net-(D1-Pad2)
- D2 pad 2: +3V3 -> Net-(D2-Pad2)
- R15 pad 2: +5V -> /USB/VBUS_0
- R44 pad 1: Net-(U2-PadD5) -> Net-(R44-Pad1)
- U1 pad A147: CAM3_DAT3- -> GBE_MDI3_P
- U1 pad B147: (no net) -> CAM3_DAT3-
- U1 pad B72: CAM2_TRIGGER -> CAM5_SDA
- U1 pad B74: CAM2_ENABLE -> CAM5_SCL
- U1 pad B75: CAM5_ENABLE -> CAM2_ENABLE
- U1 pad B77: CAM5_TRIGGER -> CAM2_TRIGGER
- U1 pad B78: CAM5_SDA -> CAM5_TRIGGER
- U1 pad B80: CAM5_SCL -> CAM5_ENABLE
- U2 pad A6: Net-(U2-PadA6) -> Net-(C63-Pad2)
- U2 pad A7: Net-(U2-PadA7) -> Net-(C64-Pad1)
- U2 pad B1: FPGA_USB0_D- -> /USB/USB_H0_D_N
- U2 pad B13: FPGA_USB1_D- -> unconnected-(U2-PadB13)
- U2 pad B14: FPGA_USB1_D+ -> unconnected-(U2-PadB14)
- U2 pad B2: FPGA_USB0_D+ -> /USB/USB_H0_D_P
- U2 pad C1: FPGA_USB0_TX+ -> /USB/USB_H0_TX_P
- U2 pad C2: FPGA_USB0_TX- -> /USB/USB_H0_TX_N
- U2 pad C6: +3V3 -> Net-(R44-Pad1)
- U2 pad D1: FPGA_USB0_RX+ -> /USB/USB_H0_RX_P
- U2 pad D2: FPGA_USB0_RX- -> /USB/USB_H0_RX_N
- U2 pad D5: Net-(U2-PadD5) -> Net-(R44-Pad1)
- U2 pad E13: FPGA_USB1_RX- -> unconnected-(U2-PadE13)
- U2 pad E14: FPGA_USB1_RX+ -> unconnected-(U2-PadE14)
- U2 pad F13: FPGA_USB1_TX- -> unconnected-(U2-PadF13)
- U2 pad F14: FPGA_USB1_TX+ -> unconnected-(U2-PadF14)
- U2 pad F5: Net-(U2-PadD5) -> Net-(R44-Pad1)
- U2 pad G13: /USB/USB_H0_RX_N -> FPGA_USB0_RX+
- U2 pad G14: /USB/USB_H0_RX_P -> FPGA_USB0_RX-
- U2 pad G5: +3V3 -> Net-(R44-Pad1)
- U2 pad H13: /USB/USB_H0_TX_N -> FPGA_USB0_TX-
- U2 pad H14: /USB/USB_H0_TX_P -> FPGA_USB0_TX+
- U2 pad J13: /USB/USB_H0_D_N -> FPGA_USB0_D-
- U2 pad J14: /USB/USB_H0_D_P -> FPGA_USB0_D+
- U2 pad J6: unconnected-(U2-PadJ6) -> /USB/USBEN0
- U2 pad K13: unconnected-(U2-PadK13) -> FPGA_USB1_D-
- U2 pad K14: unconnected-(U2-PadK14) -> FPGA_USB1_D+
- U2 pad K6: +3V3 -> /USB/nOVC0
- U2 pad L7: /USB/nOVC0 -> +3V3
- U2 pad N13: unconnected-(U2-PadN13) -> FPGA_USB1_RX+
- U2 pad N14: unconnected-(U2-PadN14) -> FPGA_USB1_RX-
- U2 pad N3: /USB/USBEN0 -> unconnected-(U2-PadN3)
- U2 pad P12: unconnected-(U2-PadP12) -> FPGA_USB1_TX-
- U2 pad P13: unconnected-(U2-PadP13) -> FPGA_USB1_TX+
- U5 pad 1: /USB/VBUS_0 -> /USB/VBUS_1
- U5 pad 10: /USB/VBUS_1 -> /USB/VBUS_0
- U5 pad 11: /USB/USB_H1_D_N -> /USB/USB_H0_D_N
- U5 pad 12: /USB/USB_H1_D_P -> /USB/USB_H0_D_P
- U5 pad 14: /USB/USB_H1_RX_N -> /USB/USB_H0_RX_N
- U5 pad 15: /USB/USB_H1_RX_P -> /USB/USB_H0_RX_P
- U5 pad 17: Net-(U5-Pad17) -> /USB/USB_H0_TX_CONN_N
- U5 pad 18: Net-(U5-Pad18) -> /USB/USB_H0_TX_CONN_P
- U5 pad 2: /USB/USB_H0_D_N -> /USB/USB_H1_D_N
- U5 pad 3: /USB/USB_H0_D_P -> /USB/USB_H1_D_P
- U5 pad 5: /USB/USB_H0_RX_N -> /USB/USB_H1_RX_N
- U5 pad 6: /USB/USB_H0_RX_P -> /USB/USB_H1_RX_P
- U5 pad 8: Net-(U5-Pad8) -> /USB/USB_H1_TX_CONN_N
- U5 pad 9: Net-(U5-Pad9) -> /USB/USB_H1_TX_CONN_P
- Y1 pad 1: Net-(U2-PadA7) -> Net-(C63-Pad2)
- Y1 pad 2: Net-(U2-PadA6) -> Net-(C64-Pad1)
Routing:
- net CAM2_DAT0-: track 0.00 -> 44.7 mm, vias 0 -> 1
- net CAM2_DAT0+: track 0.00 -> 43.4 mm, vias 0 -> 1
- net GND: track 3.41 -> 46.0 mm, vias 2 -> 29
- net CAM2_DAT1-: track 0.00 -> 41.9 mm, vias 0 -> 1
- net CAM2_DAT1+: track 0.00 -> 40.7 mm, vias 0 -> 1
- net /USB/USB_H1_TX_P: track 0.00 -> 37.2 mm, vias 0 -> 1
- net /USB/USB_H1_TX_N: track 0.00 -> 36.9 mm, vias 0 -> 1
- net /USB/USB_H1_D_N: track 0.00 -> 35.2 mm, vias 0 -> 1
- net /USB/USB_H1_D_P: track 0.00 -> 34.8 mm, vias 0 -> 1
- net FPGA_USB1_TX+: track 0.00 -> 30.7 mm
- net FPGA_USB1_TX-: track 0.00 -> 30.7 mm
- net /USB/USB_DS_RX1_N: track 0.00 -> 30.6 mm, vias 0 -> 1
- net /USB/USB_DS_RX1_P: track 0.00 -> 30.5 mm, vias 0 -> 1
- net CAM0_DAT1-: track 0.00 -> 30.1 mm, vias 0 -> 1
- net CAM0_DAT1+: track 0.00 -> 30.0 mm, vias 0 -> 1
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- added copper zone on In1.Cu, net GND
- added copper zone on In4.Cu, net GND
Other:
- board outline added: 130 x 120 mm
- copper layers 2 -> 6
